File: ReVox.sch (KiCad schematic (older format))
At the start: 41 parts, among them CN1 EXPANSION_PORT, CN2 RAW_OUT, CN4 CN_RAW_DAC, U1 GAL20V8, U2 74LS273, U3 TLC272

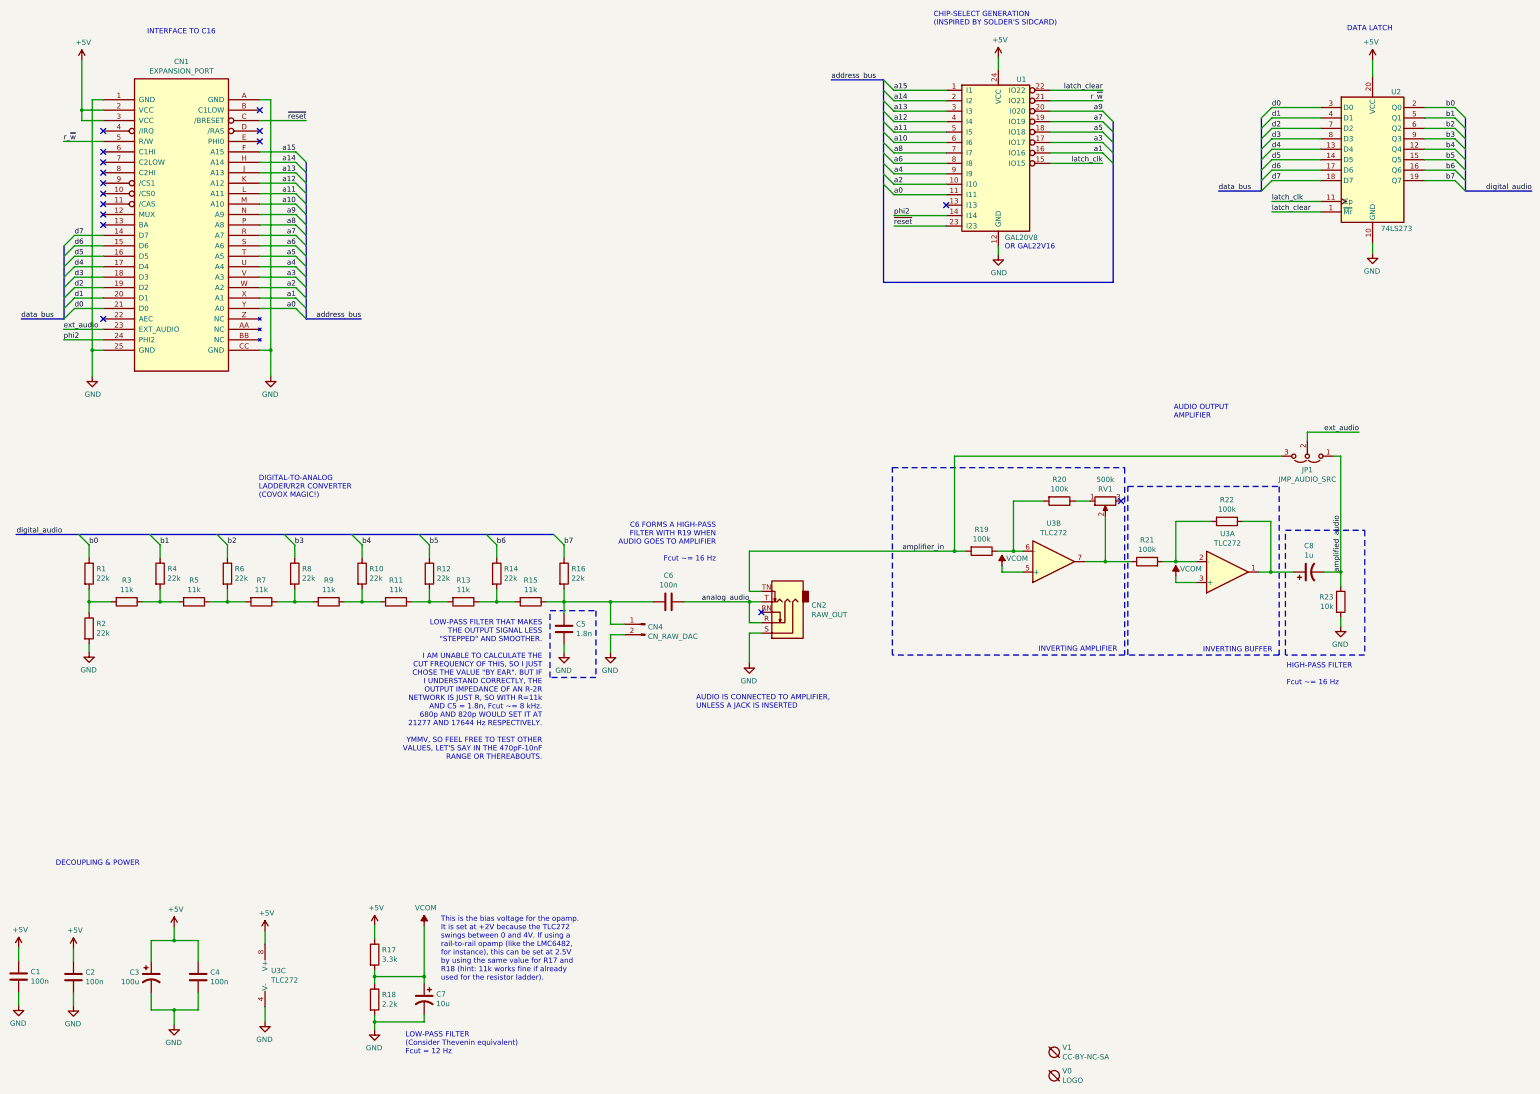
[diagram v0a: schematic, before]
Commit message: Some rerouting
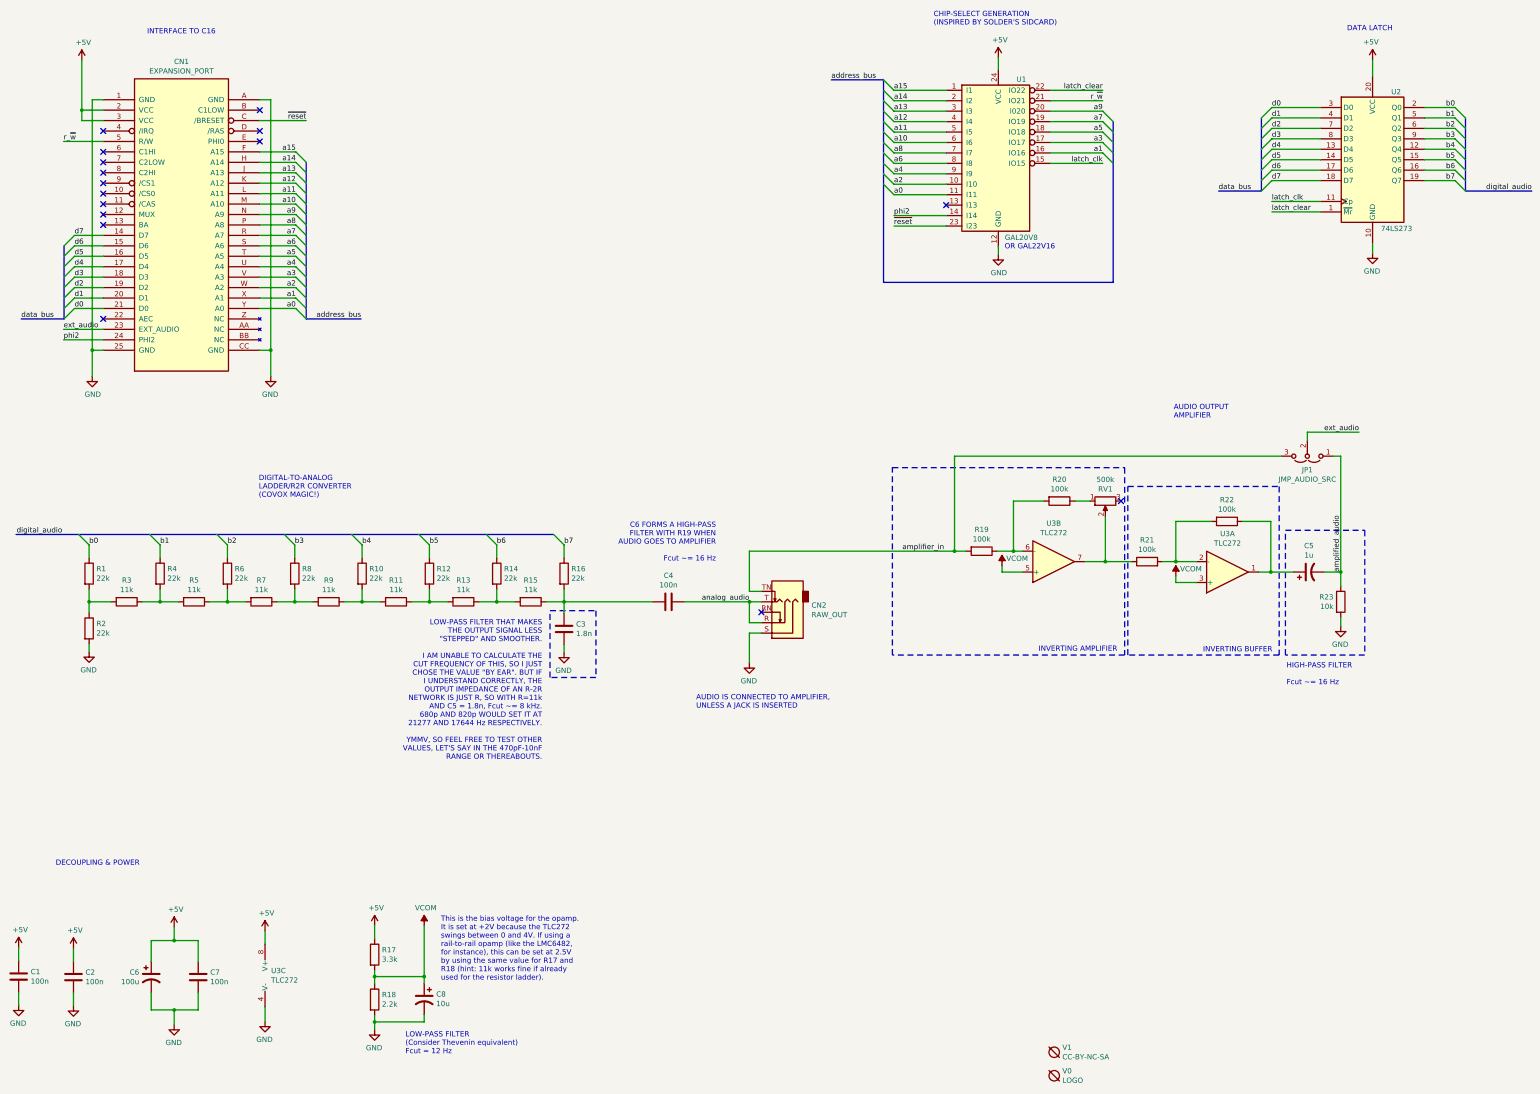
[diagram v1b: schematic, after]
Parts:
- removed CN4: CN_RAW_DAC, Connector_PinHeader_2.54mm:PinHeader_1x02_P2.54mm_Vertical, symbol Connector:Conn_01x02_Male
- renumbered C5 to C3, C6 to C4, C8 to C5, C3 to C6, C4 to C7, C7 to C8
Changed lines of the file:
@@
 	6305 6365 6305 6485
-Wire Wire Line
-	6305 6485 6750 6485
 Wire Wire Line
 	6305 6065 6305 5940
@@
 b7
 $Comp
-L Device:C C6
+L Device:C C4
 U 1 1 64B44D19
 P 7305 6485
-F 0 "C6" V 7053 6485 50  0000 C CNN
+F 0 "C4" V 7053 6485 50  0000 C CNN
 F 1 "100n" V 7144 6485 50  0000 C CNN
 F 2 "Capacitor_THT:C_Disc_D7.0mm_W2.5mm_P5.00mm" H 7343 6335 50  0001 C CNN
@@
 $EndComp
 $Comp
-L Device:C C5
+L Device:C C3
 U 1 1 64B457A8
 P 6305 6745
-F 0 "C5" H 6190 6699 50  0000 R CNN
+F 0 "C3" H 6190 6699 50  0000 R CNN
 F 1 "1.8n" H 6190 6790 50  0000 R CNN
 F 2 "Capacitor_THT:C_Disc_D7.0mm_W2.5mm_P5.00mm" H 6343 6595 50  0001 C CNN
@@
 analog_audio
 $Comp
-L Device:C C4
+L Device:C C7
 U 1 1 64B83085
 P 2800 10080
-F 0 "C4" H 2915 10126 50  0000 L CNN
+F 0 "C7" H 2915 10126 50  0000 L CNN
 F 1 "100n" H 2915 10035 50  0000 L CNN
 F 2 "Capacitor_THT:C_Disc_D7.0mm_W2.5mm_P5.00mm" H 2838 9930 50  0001 C CNN
@@
 	2350 9930 2350 9730
 $Comp
-L Device:CP1 C3
+L Device:CP1 C6
 U 1 1 64C59A52
 P 2350 10080
-F 0 "C3" H 2235 10126 50  0000 R CNN
+F 0 "C6" H 2235 10126 50  0000 R CNN
 F 1 "100u" H 2235 10035 50  0000 R CNN
 F 2 "Capacitor_THT:CP_Radial_D6.3mm_P2.50mm" H 2350 10080 50  0001 C CNN
@@
 Entry Wire Line
 	11465 1885 11565 1985
-$Comp
-L Connector:Conn_01x02_Male CN4
-U 1 1 64EEFAB7
-P 7080 6700
-F 0 "CN4" H 7052 6674 50  0000 R CNN
-F 1 "CN_RAW_DAC" H 7052 6583 50  0000 R CNN
-F 2 "Connector_PinHeader_2.54mm:PinHeader_1x02_P2.54mm_Vertical" H 7080 6700 50  0001 C CNN
-F 3 "~" H 7080 6700 50  0001 C CNN
-F 4 "-" H 7080 6700 50  0001 C CNN "MouserPN"
-F 5 "Mainly meant for debugging" H 7080 6700 50  0001 C CNN "Notes"
-	1    7080 6700
-	-1   0    0    -1
-$EndComp
-Wire Wire Line
-	6750 6485 6750 6700
-Wire Wire Line
-	6750 6700 6880 6700
-Connection ~ 6750 6485
-Wire Wire Line
-	6750 6485 7155 6485
-Wire Wire Line
-	6880 6800 6750 6800
-$Comp
-L power:GND #PWR012
-U 1 1 64F42E40
-P 6750 6970
-F 0 "#PWR012" H 6750 6720 50  0001 C CNN
-F 1 "GND" H 6755 6797 50  0000 C CNN
-F 2 "" H 6750 6970 50  0001 C CNN
-F 3 "" H 6750 6970 50  0001 C CNN
-	1    6750 6970
-	-1   0    0    -1
-$EndComp
-Wire Wire Line
-	6750 6800 6750 6970
 NoConn ~ 1890 3775
 NoConn ~ 1890 1975
@@
 P 13440 6200
 AR Path="/6579482E/65C5C61C" Ref="C?"  Part="1"
-AR Path="/65C5C61C" Ref="C8"  Part="1"
+AR Path="/65C5C61C" Ref="C5"  Part="1"
 AR Path="/65BF4077/65C5C61C" Ref="C?"  Part="1"
-F 0 "C8" V 13692 6200 50  0000 C CNN
+F 0 "C5" V 13692 6200 50  0000 C CNN
 F 1 "1u" V 13601 6200 50  0000 C CNN
 F 2 "Capacitor_THT:CP_Radial_D5.0mm_P2.00mm" H 13440 6200 50  0001 C CNN
@@
 P 4965 10290
 AR Path="/6579482E/65EB8AE6" Ref="C?"  Part="1"
-AR Path="/65EB8AE6" Ref="C7"  Part="1"
+AR Path="/65EB8AE6" Ref="C8"  Part="1"
 AR Path="/65E4CD03/65EB8AE6" Ref="C?"  Part="1"
-F 0 "C7" H 4850 10336 50  0000 R CNN
+F 0 "C8" H 4850 10336 50  0000 R CNN
 F 1 "10u" H 4850 10245 50  0000 R CNN
 F 2 "Capacitor_THT:CP_Radial_D5.0mm_P2.00mm" H 4965 10290 50  0001 C CNN
@@
 Wire Wire Line
 	13745 6200 13745 5090
+Wire Wire Line
+	6305 6485 7155 6485
 Wire Bus Line
 	11565 1885 11565 3425
